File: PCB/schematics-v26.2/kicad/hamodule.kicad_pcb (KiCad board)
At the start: 4 copper layers, 131.9 x 84.5 mm, 206 parts, among them J1 GND|5V, J10 Tx|Rx, J11 Sda|Scl, J12 3|9, J13 13|12, J14 3.3v|GND|7|15, J15 2604-1104, J16 2604-1104, J17 TestPoint, J19 TestPoint, J2 2604-1102, J3 USB_C_Receptacle_USB2.0, J4 GND|3.3V, J5 Jumper 3.3v, J6 2604-1104, J7 2604-1104, J8 5v|GND|Do, J9 Screen, K1 AQG22205, K2 AQG22205, K3 AQG22205, K4 AQG22205, K5 AQG22205, K6 AQG22205, K7 AQG22205, K8 AQG22205, SW1 USB | PS, SW2 Reset, SW3 Boot, U1 LD1117AV33, U10 SN74LV1T34DBV, U11 ULN2803A, U12 TCAL6416, U14 74AHC1G04, U2 USBLC6-2SC6, U3 ESP32-S3-WROOM-2, U4 LDA210, U5 LDA210, U6 LDA210, U7 LDA210, U8 SHT4x, U9 SN74LVCH8T245

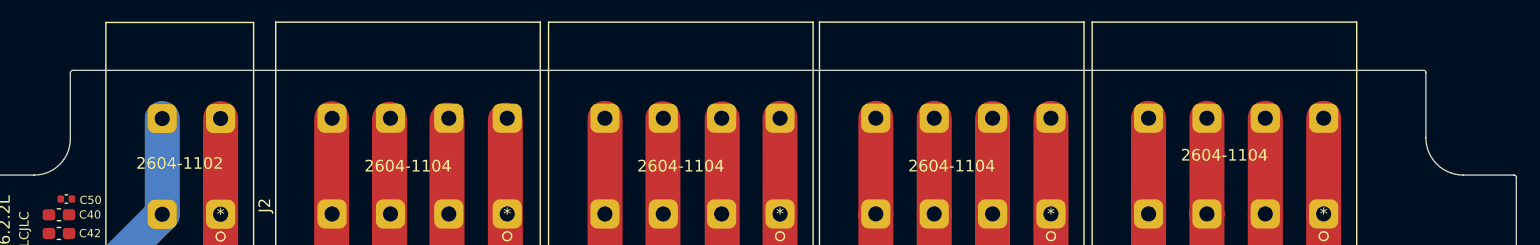
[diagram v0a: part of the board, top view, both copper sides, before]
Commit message: [26.2.2L] adjusted borders  + production files
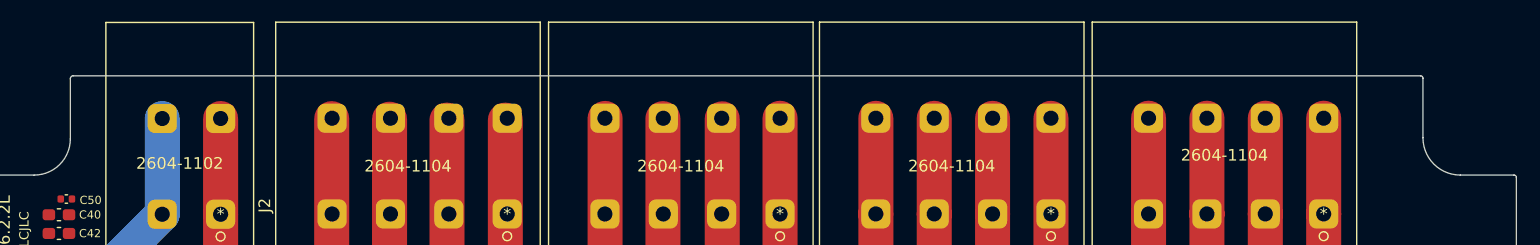
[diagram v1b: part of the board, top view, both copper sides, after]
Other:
- board size 131.9 x 84.5 mm -> 131.9 x 84 mm
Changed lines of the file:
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@@
 	)
 	(gr_line
-		(start 147.05 31.03)
-		(end 31.391411 31.03)
+		(start 146.8 31.5)
+		(end 31.391411 31.5)
 		(stroke
 			(width 0.05)
@@
 	)
 	(gr_arc
-		(start 147.05 31.03)
-		(mid 147.191421 31.088579)
-		(end 147.25 31.23)
+		(start 146.8 31.5)
+		(mid 146.941421 31.558579)
+		(end 147 31.7)
 		(stroke
 			(width 0.05)
@@
 	)
 	(gr_arc
-		(start 150.45 40)
-		(mid 148.187258 39.062742)
-		(end 147.25 36.8)
+		(start 150.2 40)
+		(mid 147.937258 39.062742)
+		(end 147 36.8)
 		(stroke
 			(width 0.05)
@@
 	(gr_line
 		(start 31.15 36.9)
-		(end 31.15 31.271411)
+		(end 31.15 31.7414)
 		(stroke
 			(width 0.05)
@@
 	)
 	(gr_line
-		(start 150.45 40)
+		(start 150.2 40)
 		(end 154.8 40)
 		(stroke
@@
 	)
 	(gr_line
-		(start 147.25 36.8)
-		(end 147.25 31.23)
+		(start 147 36.8)
+		(end 147 31.7)
 		(stroke
 			(width 0.05)
@@
 	)
 	(gr_arc
-		(start 31.15 31.271411)
-		(mid 31.220708 31.100708)
-		(end 31.391411 31.03)
+		(start 31.15 31.741411)
+		(mid 31.220708 31.570708)
+		(end 31.391411 31.5)
 		(stroke
 			(width 0.05)
@@
 		(layer "Dwgs.User")
 		(pts
-			(xy 147.05 31.03) (xy 147.05 40.03)
+			(xy 146.55 31.5) (xy 146.55 40.03)
 		)
 		(height -10.5)
@@
 			(keep_text_aligned yes)
 		)
-		(gr_text "9.0000 mm"
-			(at 156.399984 35.529993 90)
+		(gr_text "8.5300 mm"
+			(at 155.899975 35.764992 90)
 			(layer "Dwgs.User")
 			(effects
@@
 		(layer "Dwgs.User")
 		(pts
-			(xy 31.129289 32.4) (xy 147.25 32.4)
+			(xy 31.129289 32.4) (xy 147 32.399544)
 		)
 		(height -8)
@@
 			(keep_text_aligned yes)
 		)
-		(gr_text "116.1207 mm"
-			(at 88.92278 23.449989 0)
+		(gr_text "115.8707 mm"
+			(at 88.798318 23.449757 0.0002254829975)
 			(layer "Dwgs.User")
 			(effects
@@
 		(layer "Dwgs.User")
 		(pts
-			(xy 147.25 36.8) (xy 155.05 36.83)
+			(xy 147 36.8) (xy 155.05 36.83)
 		)
 		(height -12.460317)
@@
 			(keep_text_aligned yes)
 		)
-		(gr_text "7.8001 mm"
-			(at 151.202347 23.204784 359.7796327)
+		(gr_text "8.0501 mm"
+			(at 151.075722 23.204778 359.7864763)
 			(layer "Dwgs.User")
 			(effects
